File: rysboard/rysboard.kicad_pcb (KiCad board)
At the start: 4 copper layers, 56 x 65 mm, 152 parts, among them IC1 LM74801QDRRRQ1, IC2 LM74801QDRRRQ1, J1 RPi4, J10 ToF1, J11 ToF2, J12 ToF3, J13 ToF4, J15 ToF5, J16 ToF6, J19 Fan_Connector, J2 Motor L, J20 Power_SW, J22 CH1_T, J23 CH2_T, J3 Motor R, J4 Cell3, J5 Cell2, J6 Cell1, J7 Conn_01x02, J9 IMU, Q1 PMV28XPEAR, Q10 PMV28XPEAR, Q11 PMV28XPEAR, Q2 FDG6304P, Q3 NST847BDP6T5G, Q5 DMP3036SSD-13, Q6 Si7938DP-T1-GE3, Q7 NST847BDP6T5G, Q9 Si7938DP-T1-GE3, U1 L6470, U2 L6470, U3 ST1S10, U4 STM32G031K8Ux, U5 74HC2G00, U6 AP7381-33SA-7, U9 INA181

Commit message: New Layout done TODo Error Check
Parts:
- removed C17: 10u, Capacitor_SMD:C_1206_3216Metric
- removed D7: CD0603-Z3, Diode_SMD:D_0603_1608Metric
- removed D9: GREEN, LED_SMD:LED_0805_2012Metric
- removed R27: 680R, Resistor_SMD:R_0603_1608Metric
- removed R32: 100R, Resistor_SMD:R_0603_1608Metric
- removed R34: 10k1%, Resistor_SMD:R_0603_1608Metric
- removed R35: 2.8KR, Resistor_SMD:R_0603_1608Metric
- added C19: 1uF, Capacitor_SMD:C_0603_1608Metric, F.Cu at (84.0, 73.8)
- added C22: 100n, Capacitor_SMD:C_0603_1608Metric, F.Cu at (89.8, 73.8)
- added U7: AP7381-33SA-7, Package_TO_SOT_SMD:SOT-23, F.Cu at (86.8, 73.6)
- C32, Q1, Q10, Q7, R36, R52, R62, R66, R7, R70, R71, TH2: moved to B.Cu
- moved R51 88.4 mm to (93.4, 100.4), turned to 180 degrees
- moved Q11 77.7 mm to (93.4, 97.8), turned to 90 degrees
- moved R52 74.6 mm to (85.2, 112.0), turned to 270 degrees
- moved Q7 73.8 mm to (112.2, 109.7), turned to 270 degrees
- moved C29 73.3 mm to (110.8, 116.2), turned to 0 degrees
- moved R70 70.3 mm to (97.7, 119.9)
- moved R36 70.2 mm to (113.0, 97.1), turned to 270 degrees
- moved R62 69.4 mm to (90.1, 127.7)
- moved R7 63.8 mm to (114.6, 97.1), turned to 270 degrees
- moved Q1 61.6 mm to (117.3, 97.1)
- moved R66 60.2 mm to (112.3, 102.9), turned to 180 degrees
- moved C32 59.1 mm to (110.0, 106.5), turned to 180 degrees
- moved Q10 59.1 mm to (112.2, 105.4), turned to 270 degrees
- moved R71 55.2 mm to (100.9, 112.5)
- moved TH2 54.4 mm to (96.1, 109.6)
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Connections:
- net Net-(C15-Pad1) renamed /Power Supply/MCU_REG_IN
- C29 pad 1: GND -> /Power Supply/ST_Down_12V_Cap
- C29 pad 2: +12V -> GND
- J1 pad 1: +3V3 -> Net-(J1-Pad1)
- J1 pad 17: +3V3 -> Net-(J1-Pad17)
- Q1 pad 2: +12V -> +BATT
- Q5 pad 7: Net-(Q5-Pad7) -> /Power Supply/ST_Down_12V_Cap
- Q5 pad 8: Net-(Q5-Pad7) -> /Power Supply/ST_Down_12V_Cap
- R37 pad 2: Net-(Q5-Pad7) -> /Power Supply/ST_Down_12V_Cap
- R7 pad 1: +12V -> +BATT
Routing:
- net +3V3: track 155.2 -> 89.6 mm
- net +5V: track 56.2 -> 116.1 mm, vias 0 -> 1
- net /BOARD_TEMP_PROBE_1: track 36.6 -> 95.5 mm, vias 1 -> 2
- net /Power Supply/MCU_REG_IN: track 27.2 -> 82.0 mm, vias 3 -> 2
- net /VOLTAGE_PROBE_20V: track 34.4 -> 81.7 mm, vias 1 -> 2
- net Net-(Q11-Pad1): track 0.00 -> 46.2 mm, vias 0 -> 2
- net Net-(Q3-Pad2): track 22.5 -> 67.2 mm
- net Net-(C34-Pad1): track 5.42 -> 42.9 mm, vias 0 -> 2
- net Net-(Q3-Pad5): track 3.19 -> 34.3 mm
- net /VOLTAGE_PROBE_5V: track 72.4 -> 93.2 mm, vias 1 -> 2
- net /ENABLE_RAIL_12V: track 4.34 -> 25.0 mm, vias 1 -> 2
- net +BATT: track 52.4 -> 72.3 mm, vias 3 -> 14
- net Net-(IC2-Pad1): track 0.30 -> 18.7 mm, vias 0 -> 2
- net Net-(Q7-Pad6): track 0.00 -> 18.0 mm, vias 0 -> 2
- net Net-(Q10-Pad1): track 1.11 -> 17.1 mm, vias 0 -> 2
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- added copper zone on In2.Cu, net +BATT
- added copper zone on F.Cu, net /Power Supply/Battery_Balancing/V_BAT_AF_PROT-
- added copper zone on F.Cu, net /Power Supply/ST_Down_12V_Cap
- added copper zone on B.Cu, net MCU_ANALOG_SENSOR_V
- added copper zone on B.Cu, net Vdrive
- added copper zone on F.Cu, net Vdrive
- removed copper zone on F.Cu, net Net-(Q5-Pad7)

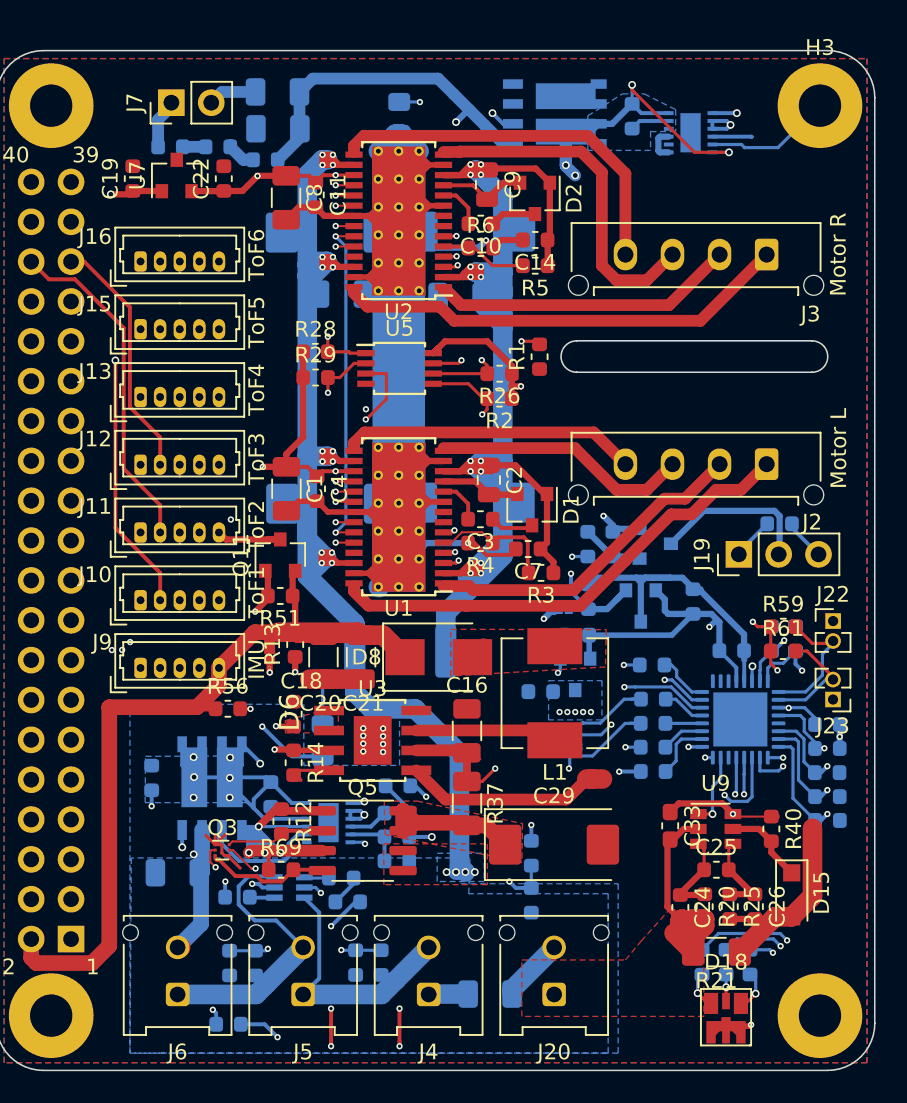
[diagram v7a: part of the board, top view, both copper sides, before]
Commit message: Labels Fixed
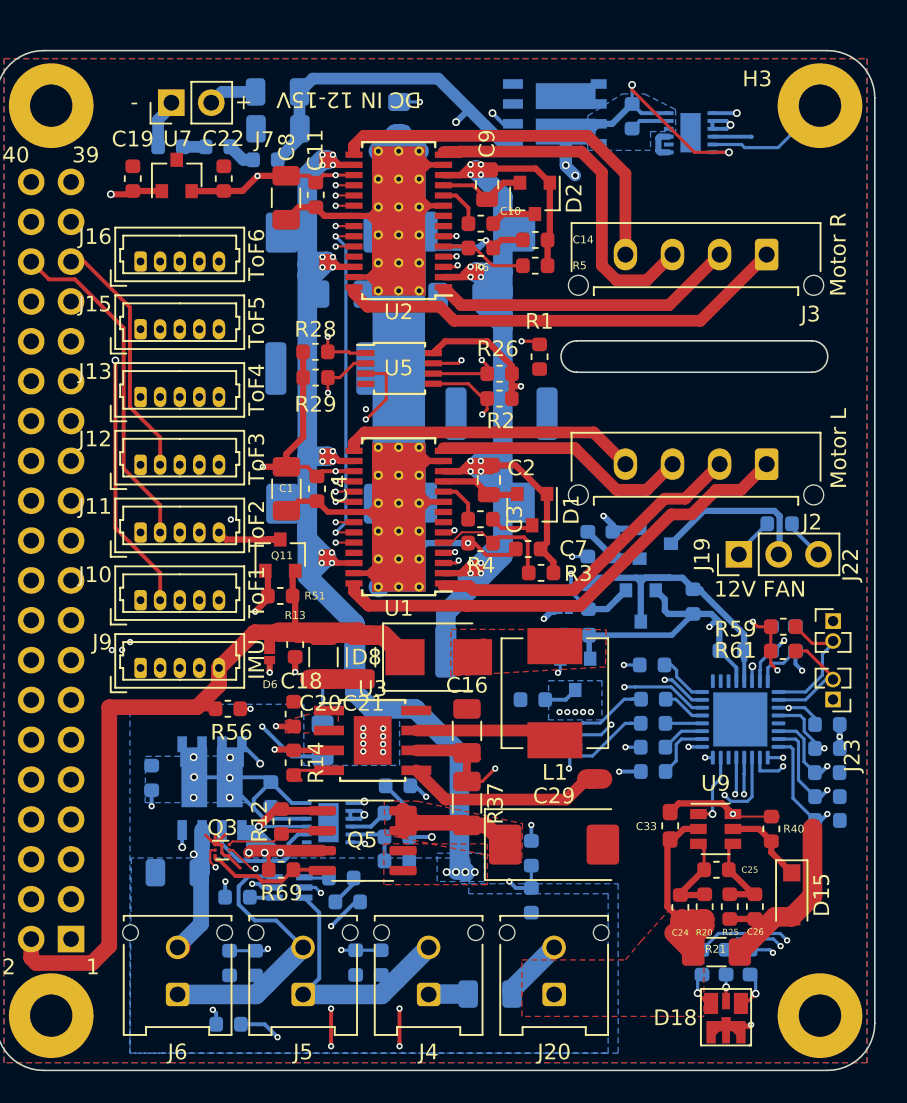
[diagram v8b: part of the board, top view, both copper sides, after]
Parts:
- added R27: R, Resistor_SMD:R_2512_6332Metric, B.Cu at (96.0, 85.9)
- added R32: R, Resistor_SMD:R_2512_6332Metric, B.Cu at (107.5, 88.8)
- moved C32 0.71 mm to (109.5, 107.0)
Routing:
- net MCU_ANALOG_SENSOR_V: track 13.2 -> 15.4 mm
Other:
- board text added: "+"
- board text added: "-"
- board text added: "12V FAN"
- board text added: "DC IN 12-15V"
